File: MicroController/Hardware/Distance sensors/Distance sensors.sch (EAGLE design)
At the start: 20 parts

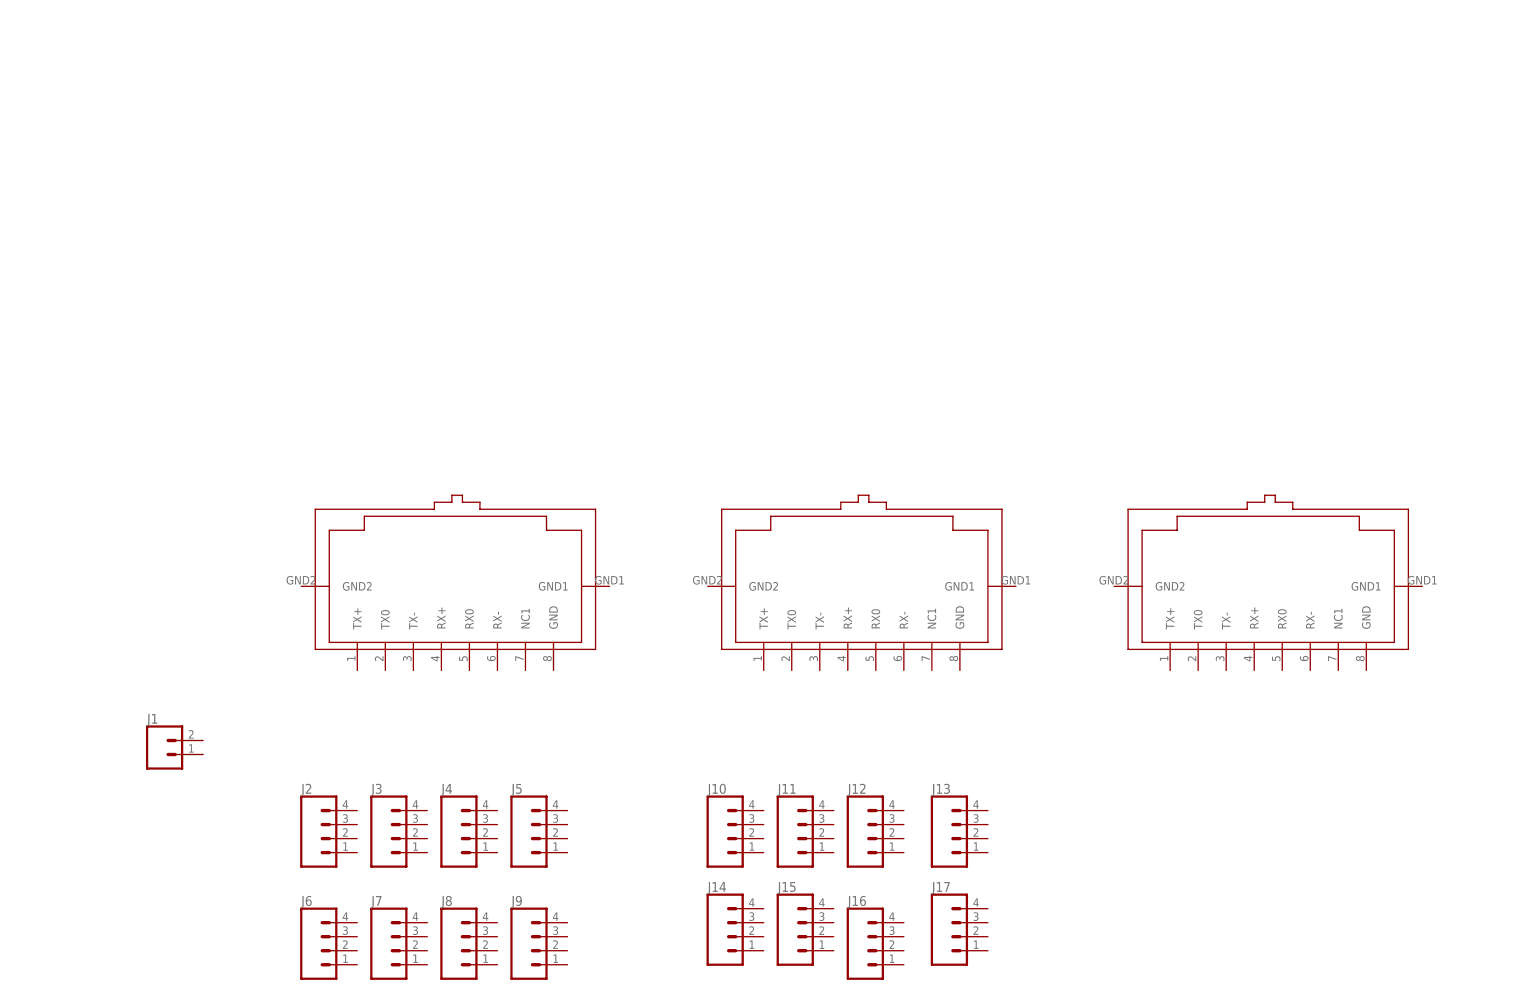
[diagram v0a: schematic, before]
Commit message: Major improvements
The Ultrasone PCB is in a good place now, it has also been well implemented on the control PCB.
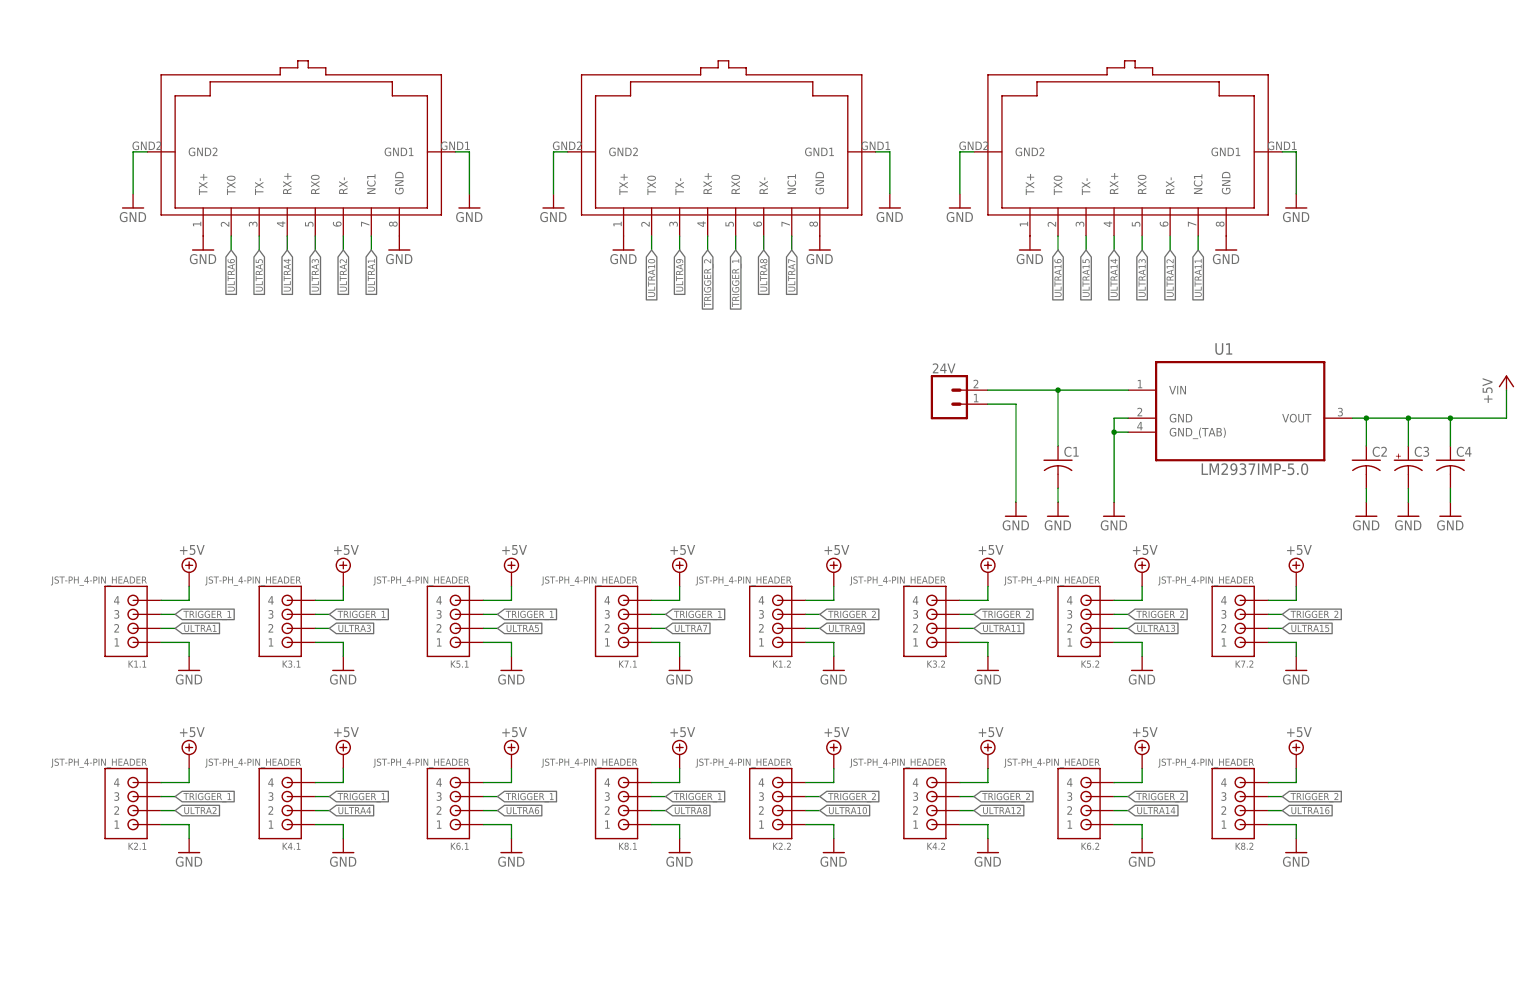
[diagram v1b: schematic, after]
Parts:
- removed J1: (no value), SparkFun-Connectors:CONN_023.5MM
- removed J10, J11, J12, J13, J14, J15, J16, J17, J2, J3, J4, J5, J6, J7, J8, J9: (no value), SparkFun-Connectors:CONN_04
- added 24V: (no value), SparkFun-Connectors:CONN_023.5MM
- added C1, C2, C4: (no value), adafruit:C-USC0805
- added C3: (no value), adafruit:CPOL-US153CLV-0505
- added K1.1, K1.2, K2.1, K2.2, K3.1, K3.2, K4.1, K4.2, K5.1, K5.2, K6.1, K6.2, K7.1, K7.2, K8.1, K8.2: JST-PH_4-PIN_HEADER, SRG:JST-PH_4-PIN_HEADER
- added U1: LM2937IMP-5.0, NSC_By_element14_Batch_1.1:LM2937IMP-5.0
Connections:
- new net +5V: C2.1, C3.+, C4.1, K1.1.4, K1.2.4, K2.1.4, K2.2.4, K3.1.4, K3.2.4, K4.1.4, K4.2.4, K5.1.4, K5.2.4, K6.1.4, K6.2.4, K7.1.4, K7.2.4, K8.1.4, K8.2.4, U1.VOUT
- new net GND: 24V.1, C1.2, C2.2, C3.-, C4.2, K1.1.1, K1.2.1, K2.1.1, K2.2.1, K3.1.1, K3.2.1, K4.1.1, K4.2.1, K5.1.1, K5.2.1, K6.1.1, K6.2.1, K7.1.1, K7.2.1, K8.1.1, K8.2.1, U$1.GND, U$1.GND1, U$1.GND2, U$1.TX+, U$2.GND, U$2.GND1, U$2.GND2, U$2.TX+, U$3.GND, U$3.GND1, U$3.GND2, U$3.TX+, U1.GND, U1.GND_(TAB)
- new net N$1: 24V.2, C1.1, U1.VIN
- new net TRIGGER_1: K1.1.3, K2.1.3, K3.1.3, K4.1.3, K5.1.3, K6.1.3, K7.1.3, K8.1.3, U$2.RX0
- new net TRIGGER_2: K1.2.3, K2.2.3, K3.2.3, K4.2.3, K5.2.3, K6.2.3, K7.2.3, K8.2.3, U$2.RX+
- new net ULTRA1: K1.1.2, U$1.NC1
- new net ULTRA10: K2.2.2, U$2.TX0
- new net ULTRA11: K3.2.2, U$3.NC1
- new net ULTRA12: K4.2.2, U$3.RX-
- new net ULTRA13: K5.2.2, U$3.RX0
- new net ULTRA14: K6.2.2, U$3.RX+
- new net ULTRA15: K7.2.2, U$3.TX-
- new net ULTRA16: K8.2.2, U$3.TX0
- new net ULTRA2: K2.1.2, U$1.RX-
- new net ULTRA3: K3.1.2, U$1.RX0
- new net ULTRA4: K4.1.2, U$1.RX+
- new net ULTRA5: K5.1.2, U$1.TX-
- new net ULTRA6: K6.1.2, U$1.TX0
- new net ULTRA7: K7.1.2, U$2.NC1
- new net ULTRA8: K8.1.2, U$2.RX-
- new net ULTRA9: K1.2.2, U$2.TX-

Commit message: Started a redesign of the Distance sensor PCB.
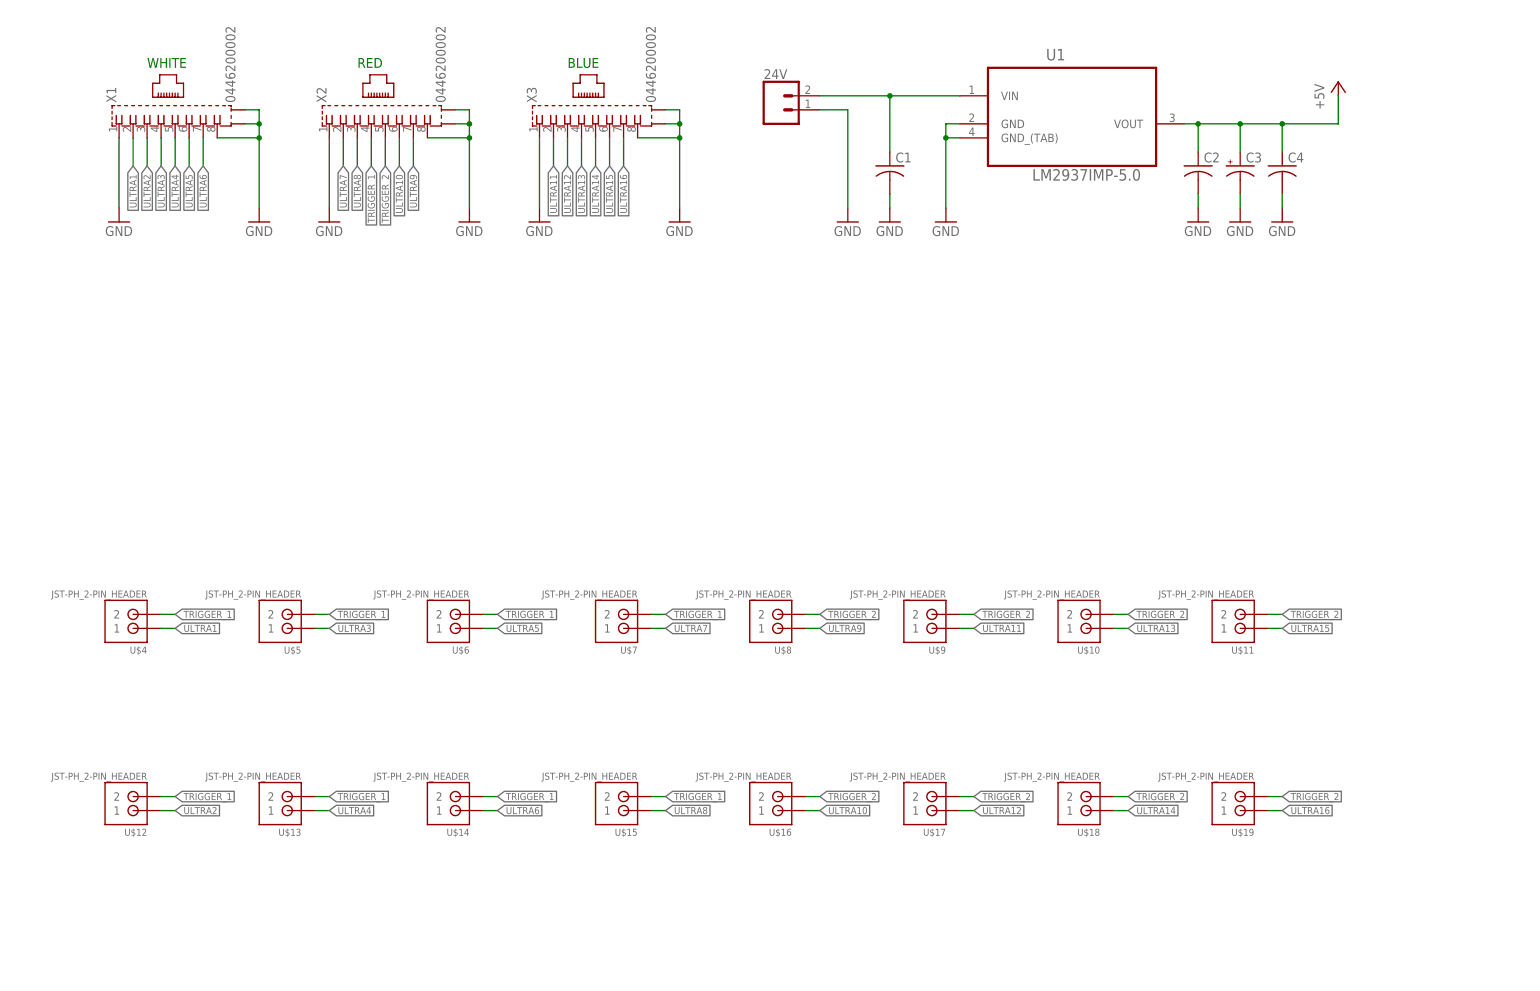
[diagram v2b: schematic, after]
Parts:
- removed K1.1, K1.2, K2.1, K2.2, K3.1, K3.2, K4.1, K4.2, K5.1, K5.2, K6.1, K6.2, K7.1, K7.2, K8.1, K8.2: JST-PH_4-PIN_HEADER, SRG:JST-PH_4-PIN_HEADER
- removed U$1, U$2, U$3: RJ45-TRAFO, con-amphenol-rj45-ld:RJ45-TRAFO
- added U$10, U$11, U$12, U$13, U$14, U$15, U$16, U$17, U$18, U$19, U$4, U$5, U$6, U$7, U$8, U$9: JST-PH_2-PIN_HEADER, SRG:JST-PH_2-PIN_HEADER
- added X1, X2, X3: 0446200002, con-molex:0446200002
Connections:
- net +5V: no longer K1.1.4, K1.2.4, K2.1.4, K2.2.4, K3.1.4, K3.2.4, K4.1.4, K4.2.4, K5.1.4, K5.2.4, K6.1.4, K6.2.4, K7.1.4, K7.2.4, K8.1.4, K8.2.4
- net GND: now also X1.1, X1.8, X1.S1, X1.S2, X2.1, X2.8, X2.S1, X2.S2, X3.1, X3.8, X3.S1, X3.S2; no longer K1.1.1, K1.2.1, K2.1.1, K2.2.1, K3.1.1, K3.2.1, K4.1.1, K4.2.1, K5.1.1, K5.2.1, K6.1.1, K6.2.1, K7.1.1, K7.2.1, K8.1.1, K8.2.1, U$1.GND, U$1.GND1, U$1.GND2, U$1.TX+, U$2.GND, U$2.GND1, U$2.GND2, U$2.TX+, U$3.GND, U$3.GND1, U$3.GND2, U$3.TX+
- net TRIGGER_1: now also U$12.2, U$13.2, U$14.2, U$15.2, U$4.2, U$5.2, U$6.2, U$7.2, X2.4; no longer K1.1.3, K2.1.3, K3.1.3, K4.1.3, K5.1.3, K6.1.3, K7.1.3, K8.1.3, U$2.RX0
- net TRIGGER_2: now also U$10.2, U$11.2, U$16.2, U$17.2, U$18.2, U$19.2, U$8.2, U$9.2, X2.5; no longer K1.2.3, K2.2.3, K3.2.3, K4.2.3, K5.2.3, K6.2.3, K7.2.3, K8.2.3, U$2.RX+
- net ULTRA1: now also U$4.1, X1.2; no longer K1.1.2, U$1.NC1
- net ULTRA10: now also U$16.1, X2.6; no longer K2.2.2, U$2.TX0
- net ULTRA11: now also U$9.1, X3.2; no longer K3.2.2, U$3.NC1
- net ULTRA12: now also U$17.1, X3.3; no longer K4.2.2, U$3.RX-
- net ULTRA13: now also U$10.1, X3.4; no longer K5.2.2, U$3.RX0
- net ULTRA14: now also U$18.1, X3.5; no longer K6.2.2, U$3.RX+
- net ULTRA15: now also U$11.1, X3.6; no longer K7.2.2, U$3.TX-
- net ULTRA16: now also U$19.1, X3.7; no longer K8.2.2, U$3.TX0
- net ULTRA2: now also U$12.1, X1.3; no longer K2.1.2, U$1.RX-
- net ULTRA3: now also U$5.1, X1.4; no longer K3.1.2, U$1.RX0
- net ULTRA4: now also U$13.1, X1.5; no longer K4.1.2, U$1.RX+
- net ULTRA5: now also U$6.1, X1.6; no longer K5.1.2, U$1.TX-
- net ULTRA6: now also U$14.1, X1.7; no longer K6.1.2, U$1.TX0
- net ULTRA7: now also U$7.1, X2.2; no longer K7.1.2, U$2.NC1
- net ULTRA8: now also U$15.1, X2.3; no longer K8.1.2, U$2.RX-
- net ULTRA9: now also U$8.1, X2.7; no longer K1.2.2, U$2.TX-
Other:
- note added: "BLUE"
- note added: "RED"
- note added: "WHITE"
- moved on the sheet: 24V, C1, C2, C3, C4, U1

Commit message: Many changes to the Ultrasone sensor PCB.
Added a lot op components.
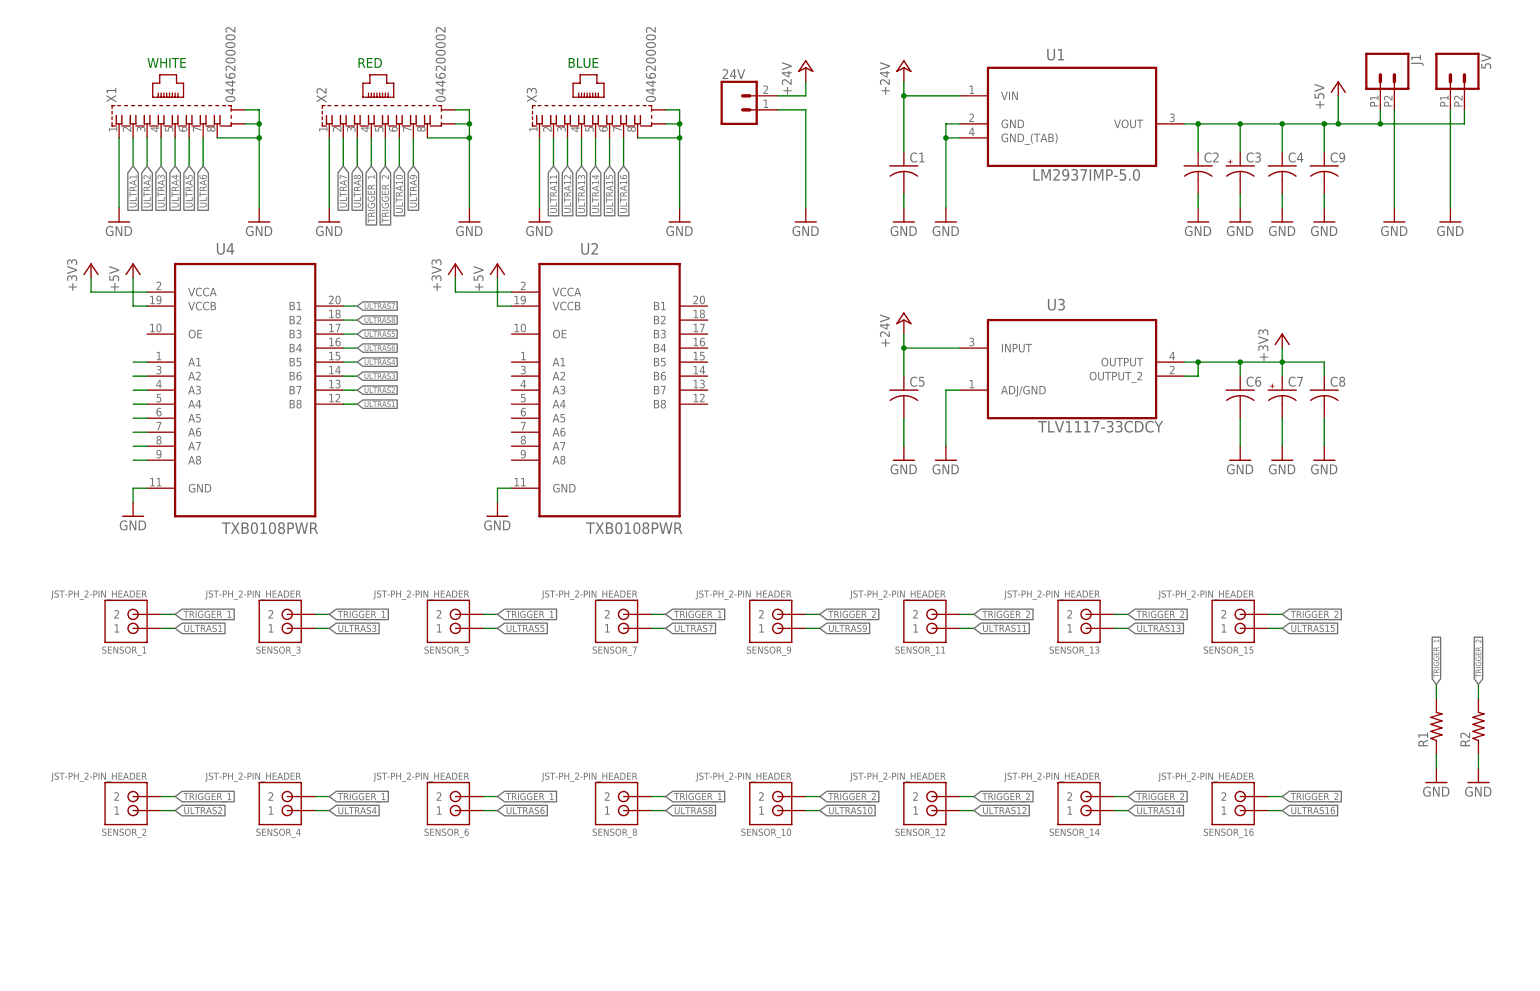
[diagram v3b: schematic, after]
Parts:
- added 5V, J1: (no value), SparkFun-Connectors:CONN_022.54MM_SCREWTERM
- added C5: (no value), adafruit:C-USC1206
- added C6, C8, C9: (no value), adafruit:C-USC0805
- added C7: (no value), adafruit:CPOL-US153CLV-0505
- added R1, R2: (no value), adafruit:R-US_R1206
- added U2, U4: TXB0108PWR, Texas Instruments_By_element14_Batch_1:TXB0108PWR
- added U3: TLV1117-33CDCY, Texas Instruments_By_element14_Batch_1:TLV1117-33CDCY
- C1: device adafruit:C-USC0805 -> adafruit:C-USC1206
- renumbered U$10 to SENSOR_13, U$11 to SENSOR_15, U$12 to SENSOR_2, U$13 to SENSOR_4, U$14 to SENSOR_6, U$15 to SENSOR_8, U$16 to SENSOR_10, U$17 to SENSOR_12, U$18 to SENSOR_14, U$19 to SENSOR_16, U$4 to SENSOR_1, U$5 to SENSOR_3, U$6 to SENSOR_5, U$7 to SENSOR_7, U$8 to SENSOR_9, U$9 to SENSOR_11
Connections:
- new net +24V: 24V.2, C1.1, C5.1, U1.VIN, U3.INPUT
- new net +3V3: C6.1, C7.+, C8.1, U2.VCCA, U3.OUTPUT, U3.OUTPUT_2, U4.VCCA
- new net N$2: U4.A2
- new net N$3: U4.A3
- new net N$4: U4.A4
- new net N$5: U4.A5
- new net N$6: U4.A6
- new net N$7: U4.A7
- new net N$8: U4.A8
- new net ULTRAS1: SENSOR_1.1, U4.B8
- new net ULTRAS10: SENSOR_10.1
- new net ULTRAS11: SENSOR_11.1
- new net ULTRAS12: SENSOR_12.1
- new net ULTRAS13: SENSOR_13.1
- new net ULTRAS14: SENSOR_14.1
- new net ULTRAS15: SENSOR_15.1
- new net ULTRAS16: SENSOR_16.1
- new net ULTRAS2: SENSOR_2.1, U4.B7
- new net ULTRAS3: SENSOR_3.1, U4.B6
- new net ULTRAS4: SENSOR_4.1, U4.B5
- new net ULTRAS5: SENSOR_5.1, U4.B3
- new net ULTRAS6: SENSOR_6.1, U4.B4
- new net ULTRAS7: SENSOR_7.1, U4.B1
- new net ULTRAS8: SENSOR_8.1, U4.B2
- new net ULTRAS9: SENSOR_9.1
- net +5V: now also 5V.2, C9.1, J1.1, U2.VCCB, U4.VCCB
- net GND: now also 5V.1, C5.2, C6.2, C7.-, C8.2, C9.2, J1.2, R1.1, R2.1, U2.GND, U3.ADJ/GND, U4.GND
- net N$1: now also U4.A1; no longer 24V.2, C1.1, U1.VIN
- net TRIGGER_1: now also R1.2
- net TRIGGER_2: now also R2.2
- net ULTRA1: no longer SENSOR_1.1
- net ULTRA10: no longer SENSOR_10.1
- net ULTRA11: no longer SENSOR_11.1
- net ULTRA12: no longer SENSOR_12.1
- net ULTRA13: no longer SENSOR_13.1
- net ULTRA14: no longer SENSOR_14.1
- net ULTRA15: no longer SENSOR_15.1
- net ULTRA16: no longer SENSOR_16.1
- net ULTRA2: no longer SENSOR_2.1
- net ULTRA3: no longer SENSOR_3.1
- net ULTRA4: no longer SENSOR_4.1
- net ULTRA5: no longer SENSOR_5.1
- net ULTRA6: no longer SENSOR_6.1
- net ULTRA7: no longer SENSOR_7.1
- net ULTRA8: no longer SENSOR_8.1
- net ULTRA9: no longer SENSOR_9.1
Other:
- moved on the sheet: 24V, C1
